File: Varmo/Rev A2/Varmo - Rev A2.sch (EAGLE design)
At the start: 104 parts, among them J1 22-05-7028-02, J2 22-05-7028-02, J3 22-05-7038-03, J4 22-05-7038-03, J5 22-05-7038-03, J6 22-05-7038-03, J7 22-05-7028-02, J8 22-05-7028-02, J9 22-05-7038-03, T1 MMBT2222AL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

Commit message: Place the new connector for the jogwheel
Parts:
- removed J8: 22-05-7028-02, con-molex:22-05-7028-02
- J7: value 22-05-7028-02 -> 22-05-7058-05; device con-molex:22-05-7028-02 -> con-molex:22-05-7058-05
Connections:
- net ESW3 renamed ESW3_TOR
- removed net ESW3_ISO: R43.2
- removed net N$15: U8.PTC11
- new net ESW3_TOR_ISO: R43.2, U8.PTA13
- new net JOGWHEEL_1: J9-2.S
- new net JOGWHEEL_2: J6-2.S
- new net WHEEL_0_LED_1: J7-1.S, U8.PTB18
- new net WHEEL_0_LED_2: J7-2.S, U8.PTB19
- new net WHEEL_1_LED_1: J7-3.S, U8.PTC0
- new net WHEEL_1_LED_2: J7-4.S, U8.PTC1
- net +3V3: now also J6-1.S, J9-1.S, U8.VDD1
- net +5V/1: now also U8.VDD2
- net DIRECTION_1: now also U8.PTC4
- net DIRECTION_2: now also U8.PTC5
- net ESW3_RX_ISO: now also U8.PTB17
- net ESW3_TX_ISO: now also U8.PTB16
- net GND1: now also J6-3.S, J9-3.S, U8.VSS
- net LED_1: now also U8.PTD3
- net LED_2: now also U8.PTD5
- net LED_STATUS_1: now also U8.PTD6
- net LED_STATUS_2: now also U8.PTD7
- net LED_STATUS_3: now also U8.PTE0
- net LED_STATUS_4: now also U8.PTE1
- net PUSH_BUTTON_1: now also U8.PTC3
- net PUSH_BUTTON_2: now also U8.PTC2
- net PWM_CONTRASTE: now also U8.PTA12
- net SCL: now also U8.PTB0
- net SDA: now also U8.PTB1
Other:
- moved on the sheet: J6-1, J6-2, J6-3, J7-1, J7-2, J9-1, J9-2, J9-3

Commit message: Route the connector jogwheel
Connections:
- net JOGWHEEL_1: now also U8.PTB3
- net JOGWHEEL_2: now also U8.PTB2
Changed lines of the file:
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@@
+</segment>
+</net>
+<net name="JOGWHEEL_1" class="0">
+<segment>
+<pinref part="U8" gate="G$1" pin="PTB3"/>
+<wire x1="160.02" y1="210.82" x2="170.18" y2="210.82" width="0.1524" layer="91"/>
+<label x="170.18" y="210.82" size="1.27" layer="95" xref="yes"/>
+</segment>
+</net>
+<net name="JOGWHEEL_2" class="0">
+<segment>
+<pinref part="U8" gate="G$1" pin="PTB2"/>
+<wire x1="160.02" y1="208.28" x2="170.18" y2="208.28" width="0.1524" layer="91"/>
+<label x="170.18" y="208.28" size="1.27" layer="95" xref="yes"/>
 </segment>
 </net>

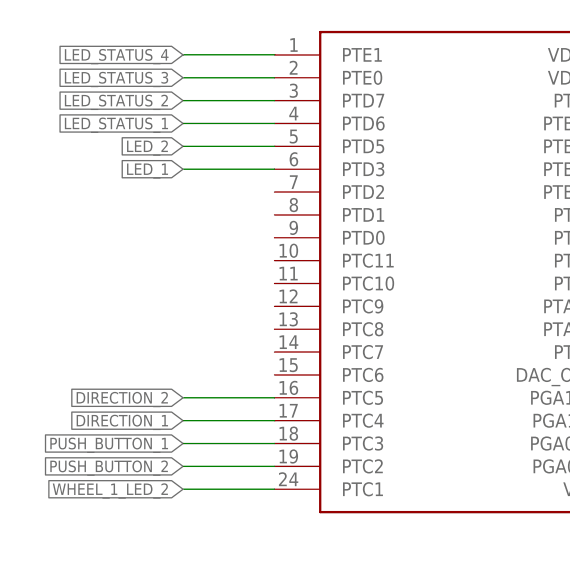
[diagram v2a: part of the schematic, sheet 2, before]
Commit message: Route the joystick connector
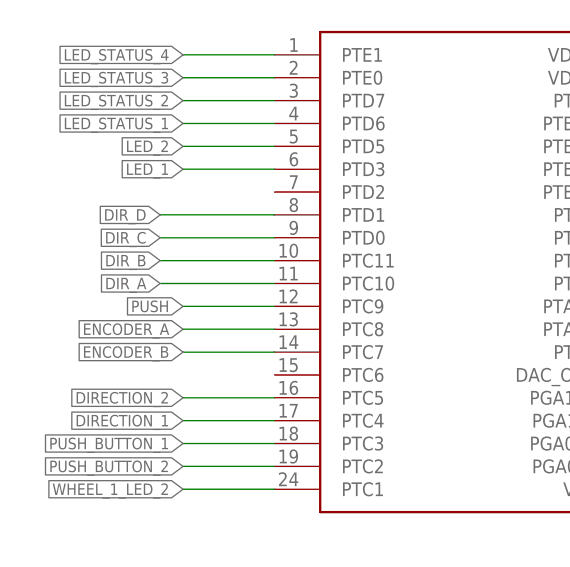
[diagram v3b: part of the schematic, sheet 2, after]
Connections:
- net DIR_A: now also U8.PTC10
- net DIR_B: now also U8.PTC11
- net DIR_C: now also U8.PTD0
- net DIR_D: now also U8.PTD1
- net ENCODER_A: now also U8.PTC8
- net ENCODER_B: now also U8.PTC7
- net PUSH: now also U8.PTC9
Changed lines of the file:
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@@
+</segment>
+</net>
+<net name="DIR_D" class="0">
+<segment>
+<wire x1="116.84" y1="210.82" x2="104.14" y2="210.82" width="0.1524" layer="91"/>
+<label x="104.14" y="210.82" size="1.27" layer="95" rot="R180" xref="yes"/>
+<pinref part="U8" gate="G$1" pin="PTD1"/>
+</segment>
+</net>
+<net name="ENCODER_A" class="0">
+<segment>
+<wire x1="116.84" y1="198.12" x2="106.68" y2="198.12" width="0.1524" layer="91"/>
+<label x="106.68" y="198.12" size="1.27" layer="95" rot="R180" xref="yes"/>
+<pinref part="U8" gate="G$1" pin="PTC8"/>
+</segment>
+</net>
+<net name="ENCODER_B" class="0">
+<segment>
+<wire x1="116.84" y1="195.58" x2="106.68" y2="195.58" width="0.1524" layer="91"/>
+<label x="106.68" y="195.58" size="1.27" layer="95" rot="R180" xref="yes"/>
+<pinref part="U8" gate="G$1" pin="PTC7"/>
+</segment>
+</net>
+<net name="PUSH" class="0">
+<segment>
+<wire x1="116.84" y1="200.66" x2="106.68" y2="200.66" width="0.1524" layer="91"/>
+<label x="106.68" y="200.66" size="1.27" layer="95" rot="R180" xref="yes"/>
+<pinref part="U8" gate="G$1" pin="PTC9"/>
+</segment>
+</net>
+<net name="DIR_A" class="0">
+<segment>
+<wire x1="116.84" y1="203.2" x2="104.14" y2="203.2" width="0.1524" layer="91"/>
+<label x="104.14" y="203.2" size="1.27" layer="95" rot="R180" xref="yes"/>
+<pinref part="U8" gate="G$1" pin="PTC10"/>
+</segment>
+</net>
+<net name="DIR_B" class="0">
+<segment>
+<wire x1="116.84" y1="205.74" x2="104.14" y2="205.74" width="0.1524" layer="91"/>
+<label x="104.14" y="205.74" size="1.27" layer="95" rot="R180" xref="yes"/>
+<pinref part="U8" gate="G$1" pin="PTC11"/>
+</segment>
+</net>
+<net name="DIR_C" class="0">
+<segment>
+<wire x1="116.84" y1="208.28" x2="104.14" y2="208.28" width="0.1524" layer="91"/>
+<label x="104.14" y="208.28" size="1.27" layer="95" rot="R180" xref="yes"/>
+<pinref part="U8" gate="G$1" pin="PTD0"/>
 </segment>
 </net>

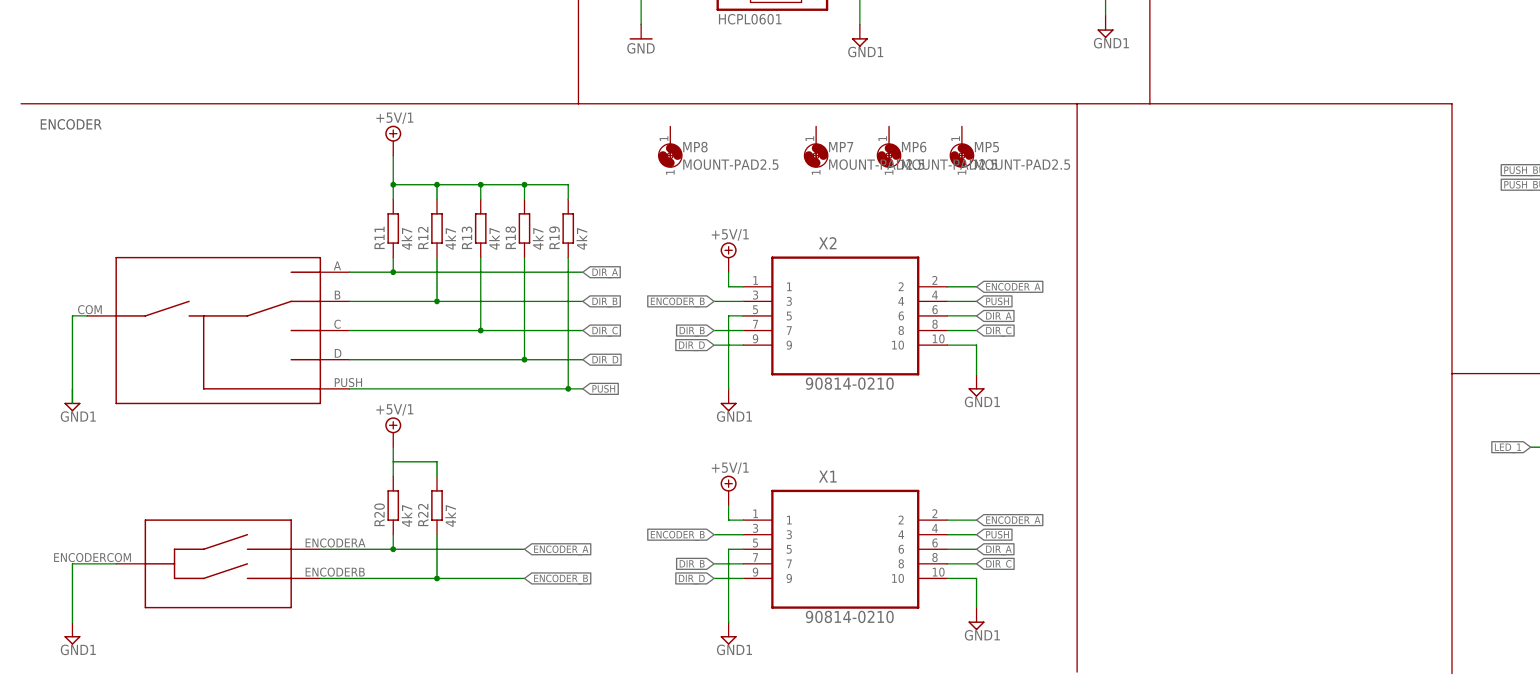
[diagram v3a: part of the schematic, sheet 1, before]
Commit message: Route the joystick/encoder board
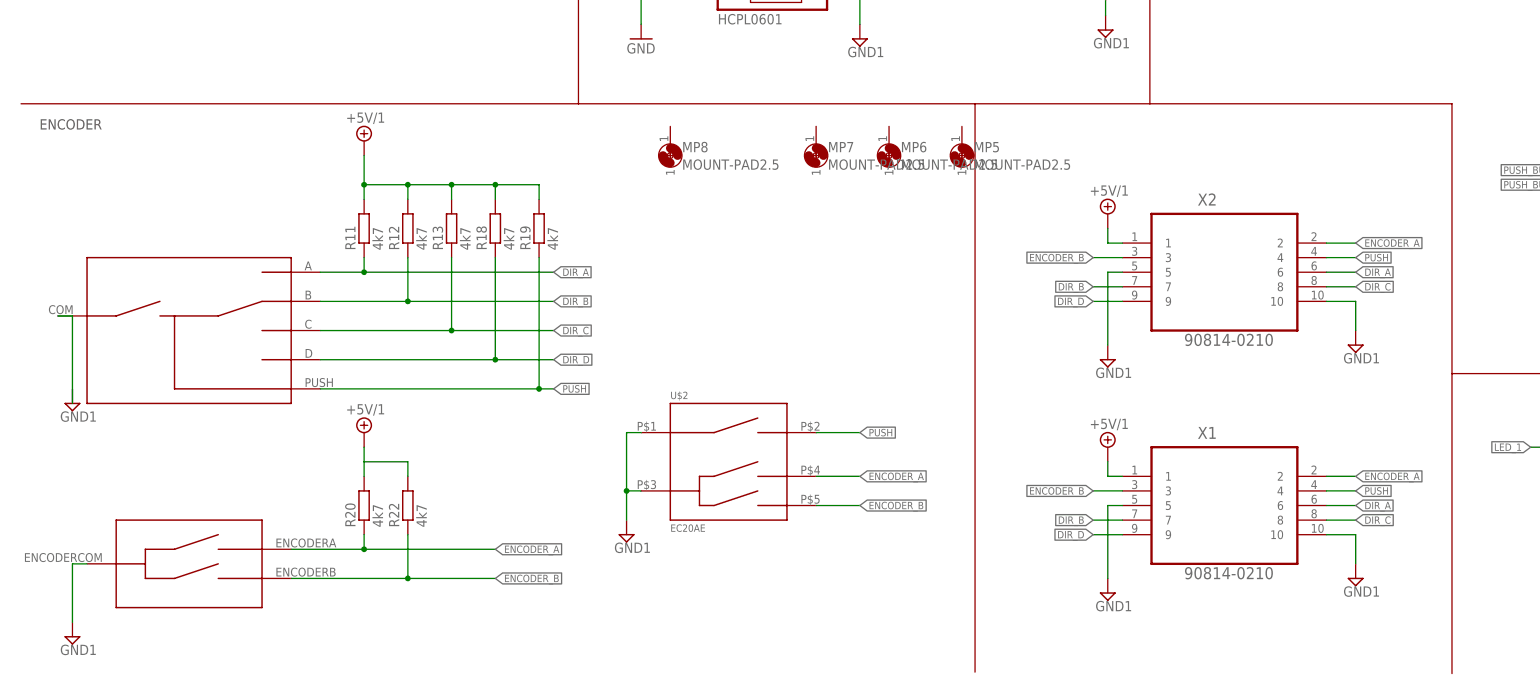
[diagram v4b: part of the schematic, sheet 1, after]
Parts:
- added U$2: EC20AE, encoder:EC20AE
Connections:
- net ENCODER_A: now also U$2.P$4
- net ENCODER_B: now also U$2.P$5
- net GND1: now also U$2.P$1, U$2.P$3
- net PUSH: now also U$2.P$2
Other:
- moved on the sheet: R11, R12, R13, R18, R19, R20, R22, X1, X2

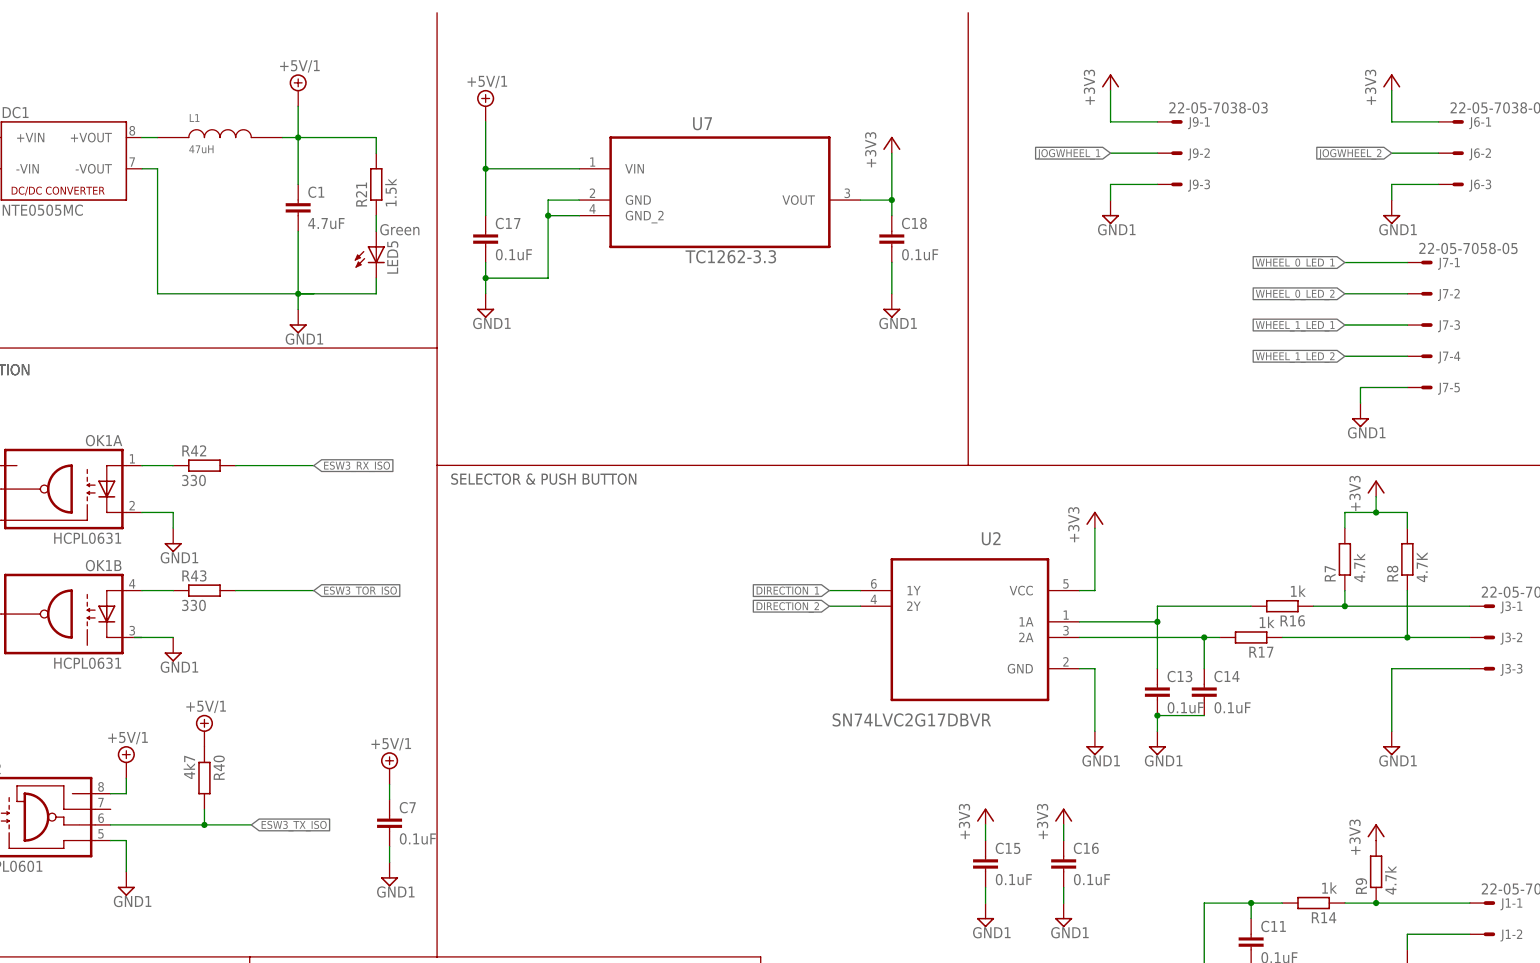
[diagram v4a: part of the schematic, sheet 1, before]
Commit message: Routing the +3V3 and the +5V/1 power
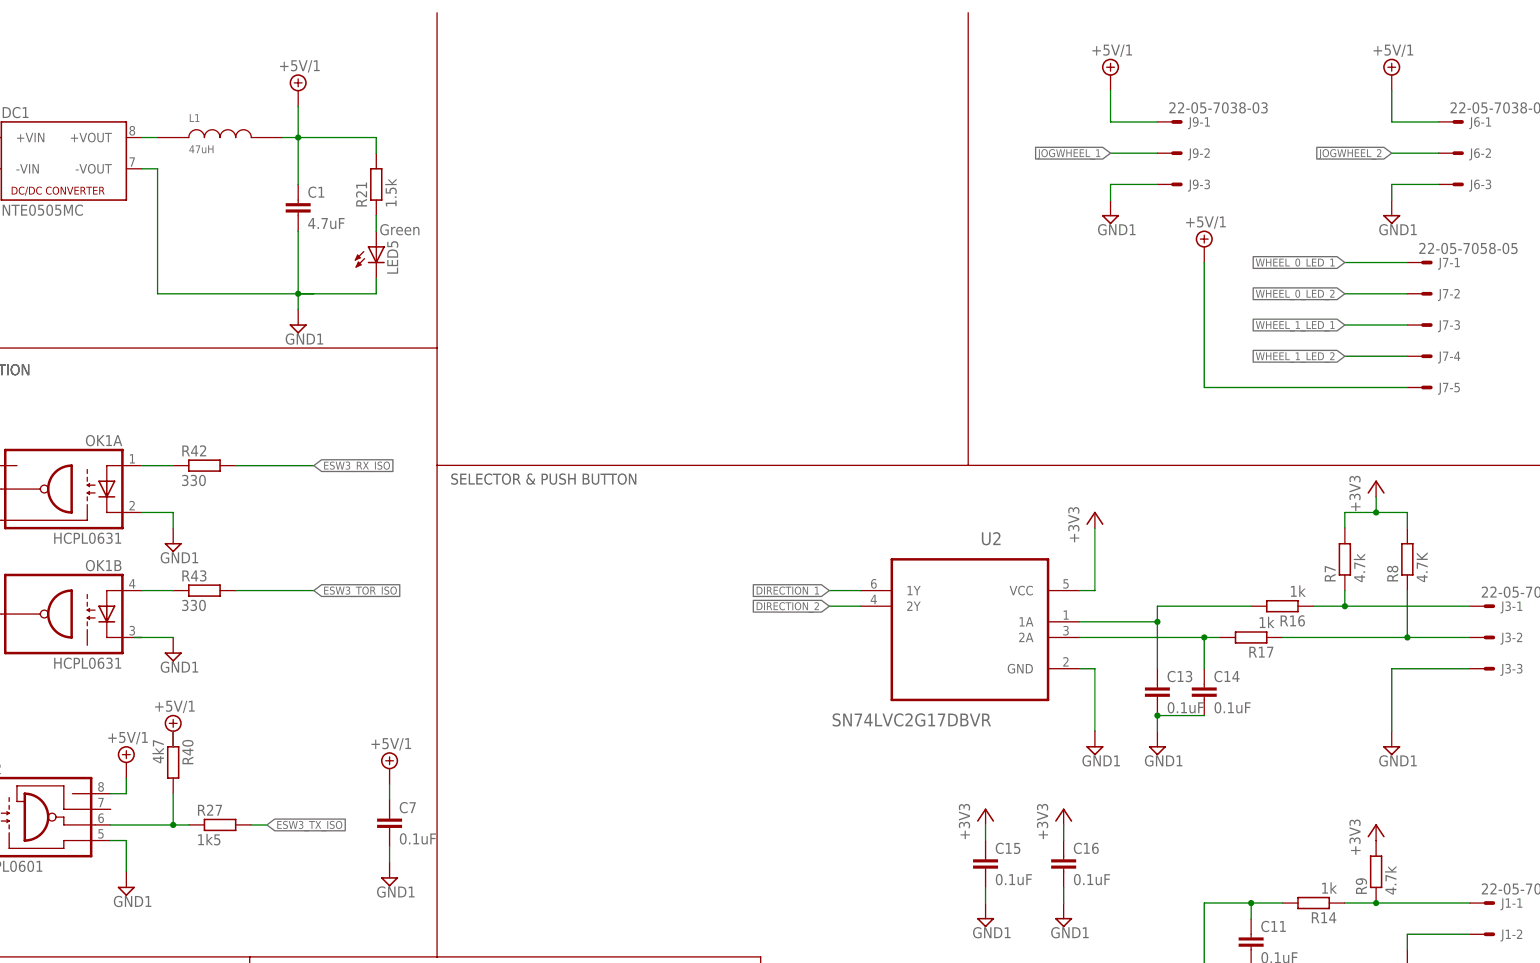
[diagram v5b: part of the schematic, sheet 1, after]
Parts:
- removed C17, C18: 0.1uF, rcl:C-EUC0603
- removed U7: TC1262-3.3, microchip-6:TC1262-3.3
- added R27: 1k5, rcl:R-EU_R0603
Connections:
- new net N$15: OK2.VO, R27.1, R40.2
- net +3V3: no longer C18.1, J6-1.S, J9-1.S, U7.VOUT
- net +5V/1: now also J6-1.S, J7-5.S, J9-1.S; no longer C17.1, U7.VIN
- net ESW3_TX_ISO: now also R27.2; no longer OK2.VO, R40.2
- net GND1: no longer C17.2, C18.2, U7.GND, U7.GND_2
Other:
- moved on the sheet: R40

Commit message: Place the logo and the CC on each board
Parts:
- added U$3, U$7: EXMACHINA-LOGO-NAME, exmachina:EXMACHINA-LOGO-NAME
- added U$4, U$5: CC-BY-NC-SA, cc-by-sa:CC-BY-NC-SA
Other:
- note removed: "ENCODER"

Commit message: Add fiducial to the schematic
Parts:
- added JP1, JP2, JP3, JP4: FIDUCIAL1X2, SparkFun:FIDUCIAL1X2
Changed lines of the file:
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@@
 <part name="U$3" library="exmachina" deviceset="EXMACHINA-LOGO" device="-NAME"/>
 <part name="U$4" library="cc-by-sa" deviceset="CC-BY-NC-SA" device=""/>
+<part name="JP1" library="SparkFun" deviceset="FIDUCIAL" device="1X2"/>
+<part name="JP2" library="SparkFun" deviceset="FIDUCIAL" device="1X2"/>
+<part name="JP3" library="SparkFun" deviceset="FIDUCIAL" device="1X2"/>
+<part name="JP4" library="SparkFun" deviceset="FIDUCIAL" device="1X2"/>
 </parts>
 <sheets>
@@
 <instance part="MP3" gate="1" x="238.76" y="10.16"/>
 <instance part="MP4" gate="1" x="261.62" y="10.16"/>
+<instance part="JP1" gate="G$1" x="344.932" y="21.844"/>
+<instance part="JP2" gate="G$1" x="348.742" y="21.844"/>
+<instance part="JP3" gate="G$1" x="352.552" y="21.844"/>
+<instance part="JP4" gate="G$1" x="356.616" y="21.844"/>
 </instances>
 <busses>
